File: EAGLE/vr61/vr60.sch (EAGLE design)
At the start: 227 parts, among them IC1 MC74VHC1G50, IC2 REG1117, J3 JTAG, J6 MICROMOD-2222-C

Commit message: pcb tracing done
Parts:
- J3: value JTAG -> (none); device SparkFun-Connectors:CORTEX_JTAG_DEBUG_MINIMUM_PTH -> SparkFun-Connectors:CONN_04
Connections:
- new net A0: J3.3, J6.A0
- new net PWM: J3.2, J6.PWM0
- net !RESET: no longer J3.!RESET
- net GND: now also J3.1; no longer J3.GND
- net SWDCK: no longer J3.SWDCLK
- net SWDIO: no longer J3.SWDIO
- net VCC: now also J3.4; no longer J3.VCC
- net VSUP: now also J6.USB_VIN
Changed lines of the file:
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@@
 <part name="JP1" library="SparkFun-Jumpers" library_urn="urn:adsk.eagle:library:528" deviceset="JUMPER-SMT_2_NC_PASTE" device="_NO-SILK" package3d_urn="urn:adsk.eagle:package:39283/1" value="OPT"/>
 <part name="J1" library="SparkFun-Connectors" library_urn="urn:adsk.eagle:library:513" deviceset="CONN_02" device="" package3d_urn="urn:adsk.eagle:package:38039/1"/>
-<part name="J3" library="SparkFun-Connectors" deviceset="CORTEX_JTAG_DEBUG_MINIMUM" device="_PTH" value="JTAG"/>
 <part name="GND10" library="ts_custom_nick_nacks" deviceset="GND" device=""/>
-<part name="GND11" library="ts_custom_nick_nacks" deviceset="GND" device=""/>
-<part name="U$18" library="ts_custom_nick_nacks" deviceset="3V3" device=""/>
+<part name="J3" library="SparkFun-Connectors" library_urn="urn:adsk.eagle:library:513" deviceset="CONN_04" device="" package3d_urn="urn:adsk.eagle:package:38085/1"/>
+<part name="U$4" library="ts_custom_nick_nacks" deviceset="3V3" device=""/>
+<part name="GND5" library="ts_custom_nick_nacks" deviceset="GND" device=""/>
 </parts>
 <sheets>
@@
 <attribute name="NAME" x="261.62" y="162.052" size="1.778" layer="95" font="vector" rot="R180"/>
 </instance>
-<instance part="J3" gate="G$1" x="241.3" y="50.8" smashed="yes" rot="R180">
-<attribute name="NAME" x="251.46" y="42.926" size="1.778" layer="95" font="vector" rot="R180"/>
-<attribute name="VALUE" x="251.46" y="58.166" size="1.778" layer="96" font="vector" rot="R180"/>
-</instance>
 <instance part="GND10" gate="1" x="248.92" y="162.56" smashed="yes">
 <attribute name="VALUE" x="248.92" y="157.988" size="1.778" layer="96" align="top-center"/>
 </instance>
-<instance part="GND11" gate="1" x="261.62" y="50.8" smashed="yes">
-<attribute name="VALUE" x="261.62" y="46.228" size="1.778" layer="96" align="top-center"/>
-</instance>
-<instance part="U$18" gate="G$1" x="256.54" y="43.18" smashed="yes" rot="R180">
-<attribute name="VALUE" x="256.54" y="38.608" size="1.778" layer="96" rot="R180" align="bottom-center"/>
+<instance part="J3" gate="G$1" x="241.3" y="55.88" smashed="yes">
+<attribute name="VALUE" x="236.22" y="48.514" size="1.778" layer="96" font="vector"/>
+<attribute name="NAME" x="236.22" y="64.008" size="1.778" layer="95" font="vector"/>
+</instance>
+<instance part="U$4" gate="G$1" x="248.92" y="63.5" smashed="yes">
+<attribute name="VALUE" x="248.92" y="68.072" size="1.778" layer="96" align="bottom-center"/>
+</instance>
+<instance part="GND5" gate="1" x="248.92" y="50.8" smashed="yes">
+<attribute name="VALUE" x="248.92" y="46.228" size="1.778" layer="96" align="top-center"/>
 </instance>
 </instances>
@@
 </segment>
 <segment>
-<pinref part="J3" gate="G$1" pin="GND"/>
-<pinref part="GND11" gate="1" pin="GND"/>
-<wire x1="261.62" y1="50.8" x2="261.62" y2="53.34" width="0.1524" layer="91"/>
-<wire x1="261.62" y1="53.34" x2="254" y2="53.34" width="0.1524" layer="91"/>
-</segment>
-<segment>
 <pinref part="J1" gate="G$1" pin="2"/>
 <wire x1="251.46" y1="165.1" x2="248.92" y2="165.1" width="0.1524" layer="91"/>
 <pinref part="GND10" gate="1" pin="GND"/>
 <wire x1="248.92" y1="165.1" x2="248.92" y2="162.56" width="0.1524" layer="91"/>
+</segment>
+<segment>
+<pinref part="J3" gate="G$1" pin="1"/>
+<wire x1="246.38" y1="53.34" x2="248.92" y2="53.34" width="0.1524" layer="91"/>
+<pinref part="GND5" gate="1" pin="GND"/>
+<wire x1="248.92" y1="53.34" x2="248.92" y2="50.8" width="0.1524" layer="91"/>
 </segment>
 </net>
@@
 </segment>
 <segment>
-<pinref part="J3" gate="G$1" pin="VCC"/>
-<wire x1="254" y1="45.72" x2="256.54" y2="45.72" width="0.1524" layer="91"/>
-<wire x1="256.54" y1="45.72" x2="256.54" y2="43.18" width="0.1524" layer="91"/>
-<pinref part="U$18" gate="G$1" pin="VCC"/>
+<pinref part="J3" gate="G$1" pin="4"/>
+<wire x1="246.38" y1="60.96" x2="248.92" y2="60.96" width="0.1524" layer="91"/>
+<pinref part="U$4" gate="G$1" pin="VCC"/>
+<wire x1="248.92" y1="60.96" x2="248.92" y2="63.5" width="0.1524" layer="91"/>
 </segment>
 </net>
@@
 <segment>
 <pinref part="J6" gate="J1" pin="AUD_OUT/CAM_MCLK"/>
-<wire x1="177.8" y1="106.68" x2="160.02" y2="106.68" width="0.1524" layer="91"/>
-<label x="160.02" y="106.68" size="1.778" layer="95" rot="R180" xref="yes"/>
+<wire x1="177.8" y1="106.68" x2="157.48" y2="106.68" width="0.1524" layer="91"/>
+<label x="157.48" y="106.68" size="1.778" layer="95" rot="R180" xref="yes"/>
 </segment>
 </net>
@@
 <segment>
 <pinref part="J6" gate="J1" pin="AUD_LRCLK"/>
-<wire x1="177.8" y1="101.6" x2="160.02" y2="101.6" width="0.1524" layer="91"/>
-<label x="160.02" y="101.6" size="1.778" layer="95" rot="R180" xref="yes"/>
+<wire x1="177.8" y1="101.6" x2="157.48" y2="101.6" width="0.1524" layer="91"/>
+<label x="157.48" y="101.6" size="1.778" layer="95" rot="R180" xref="yes"/>
 </segment>
 </net>
@@
 <segment>
 <pinref part="J6" gate="J1" pin="G3/BUS3"/>
-<wire x1="223.52" y1="86.36" x2="241.3" y2="86.36" width="0.1524" layer="91"/>
-<label x="241.3" y="86.36" size="1.778" layer="95" xref="yes"/>
+<wire x1="223.52" y1="86.36" x2="243.84" y2="86.36" width="0.1524" layer="91"/>
+<label x="243.84" y="86.36" size="1.778" layer="95" xref="yes"/>
 </segment>
 </net>
@@
 <segment>
 <pinref part="J6" gate="J1" pin="G1/BUS1"/>
-<wire x1="223.52" y1="91.44" x2="241.3" y2="91.44" width="0.1524" layer="91"/>
-<label x="241.3" y="91.44" size="1.778" layer="95" xref="yes"/>
+<wire x1="223.52" y1="91.44" x2="243.84" y2="91.44" width="0.1524" layer="91"/>
+<label x="243.84" y="91.44" size="1.778" layer="95" xref="yes"/>
 </segment>
 </net>
@@
 <segment>
 <pinref part="J6" gate="J1" pin="D1/CAM_TRIG"/>
-<wire x1="223.52" y1="116.84" x2="241.3" y2="116.84" width="0.1524" layer="91"/>
-<label x="241.3" y="116.84" size="1.778" layer="95" xref="yes"/>
+<wire x1="223.52" y1="116.84" x2="243.84" y2="116.84" width="0.1524" layer="91"/>
+<label x="243.84" y="116.84" size="1.778" layer="95" xref="yes"/>
 </segment>
 </net>
@@
 <segment>
 <pinref part="J6" gate="J1" pin="I2C_SDA"/>
-<wire x1="177.8" y1="91.44" x2="160.02" y2="91.44" width="0.1524" layer="91"/>
-<label x="160.02" y="91.44" size="1.778" layer="95" rot="R180" xref="yes"/>
+<wire x1="177.8" y1="91.44" x2="157.48" y2="91.44" width="0.1524" layer="91"/>
+<label x="157.48" y="91.44" size="1.778" layer="95" rot="R180" xref="yes"/>
 </segment>
 </net>
@@
 <segment>
 <pinref part="J6" gate="J1" pin="RX1"/>
-<wire x1="223.52" y1="109.22" x2="241.3" y2="109.22" width="0.1524" layer="91"/>
-<label x="241.3" y="109.22" size="1.778" layer="95" xref="yes"/>
+<wire x1="223.52" y1="109.22" x2="243.84" y2="109.22" width="0.1524" layer="91"/>
+<label x="243.84" y="109.22" size="1.778" layer="95" xref="yes"/>
 </segment>
 </net>
@@
 <wire x1="60.96" y1="63.5" x2="60.96" y2="66.04" width="0.1524" layer="91"/>
 </segment>
+<segment>
+<pinref part="J6" gate="J1" pin="USB_VIN"/>
+<wire x1="177.8" y1="142.24" x2="160.02" y2="142.24" width="0.1524" layer="91"/>
+<label x="160.02" y="142.24" size="1.778" layer="95" rot="MR0" xref="yes"/>
+</segment>
 </net>
 <net name="N$67" class="0">
@@
 <segment>
 <pinref part="J6" gate="J1" pin="USB_D-"/>
-<wire x1="177.8" y1="139.7" x2="170.18" y2="139.7" width="0.1524" layer="91"/>
-<label x="170.18" y="139.7" size="1.778" layer="95" rot="R180" xref="yes"/>
+<wire x1="177.8" y1="139.7" x2="167.64" y2="139.7" width="0.1524" layer="91"/>
+<label x="167.64" y="139.7" size="1.778" layer="95" rot="R180" xref="yes"/>
 </segment>
 <segment>
@@
 <segment>
 <pinref part="J6" gate="J1" pin="PWM1"/>
-<wire x1="223.52" y1="121.92" x2="241.3" y2="121.92" width="0.1524" layer="91"/>
-<label x="241.3" y="121.92" size="1.778" layer="95" xref="yes"/>
+<wire x1="223.52" y1="121.92" x2="243.84" y2="121.92" width="0.1524" layer="91"/>
+<label x="243.84" y="121.92" size="1.778" layer="95" xref="yes"/>
 </segment>
 <segment>
@@
 <net name="SWDIO" class="0">
 <segment>
-<label x="220.98" y="48.26" size="1.27" layer="95" rot="R180" xref="yes"/>
-<wire x1="231.14" y1="48.26" x2="220.98" y2="48.26" width="0.1524" layer="91"/>
-<pinref part="J3" gate="G$1" pin="SWDIO"/>
-</segment>
-<segment>
 <pinref part="J6" gate="J1" pin="SWDIO"/>
 <wire x1="177.8" y1="116.84" x2="160.02" y2="116.84" width="0.1524" layer="91"/>
@@
 <net name="SWDCK" class="0">
 <segment>
-<label x="228.6" y="50.8" size="1.27" layer="95" rot="R180" xref="yes"/>
-<wire x1="231.14" y1="50.8" x2="228.6" y2="50.8" width="0.1524" layer="91"/>
-<pinref part="J3" gate="G$1" pin="SWDCLK"/>
-</segment>
-<segment>
 <pinref part="J6" gate="J1" pin="SWDCK"/>
 <wire x1="177.8" y1="114.3" x2="172.72" y2="114.3" width="0.1524" layer="91"/>
@@
 </net>
 <net name="!RESET" class="0">
-<segment>
-<wire x1="231.14" y1="45.72" x2="228.6" y2="45.72" width="0.1524" layer="91"/>
-<label x="228.6" y="45.72" size="1.27" layer="95" rot="R180" xref="yes"/>
-<pinref part="J3" gate="G$1" pin="!RESET"/>
-</segment>
 <segment>
 <pinref part="J6" gate="J1" pin="!RESET!"/>
@@
 </segment>
 </net>
+<net name="PWM" class="0">
+<segment>
+<pinref part="J6" gate="J1" pin="PWM0"/>
+<wire x1="223.52" y1="124.46" x2="251.46" y2="124.46" width="0.1524" layer="91"/>
+<label x="251.46" y="124.46" size="1.778" layer="95" xref="yes"/>
+</segment>
+<segment>
+<pinref part="J3" gate="G$1" pin="2"/>
+<wire x1="246.38" y1="55.88" x2="248.92" y2="55.88" width="0.1524" layer="91"/>
+<label x="248.92" y="55.88" size="1.778" layer="95" xref="yes"/>
+</segment>
+</net>
+<net name="A0" class="0">
+<segment>
+<pinref part="J6" gate="J1" pin="A0"/>
+<wire x1="223.52" y1="129.54" x2="243.84" y2="129.54" width="0.1524" layer="91"/>
+<label x="243.84" y="129.54" size="1.778" layer="95" xref="yes"/>
+</segment>
+<segment>
+<pinref part="J3" gate="G$1" pin="3"/>
+<wire x1="246.38" y1="58.42" x2="259.08" y2="58.42" width="0.1524" layer="91"/>
+<label x="259.08" y="58.42" size="1.778" layer="95" xref="yes"/>
+</segment>
+</net>

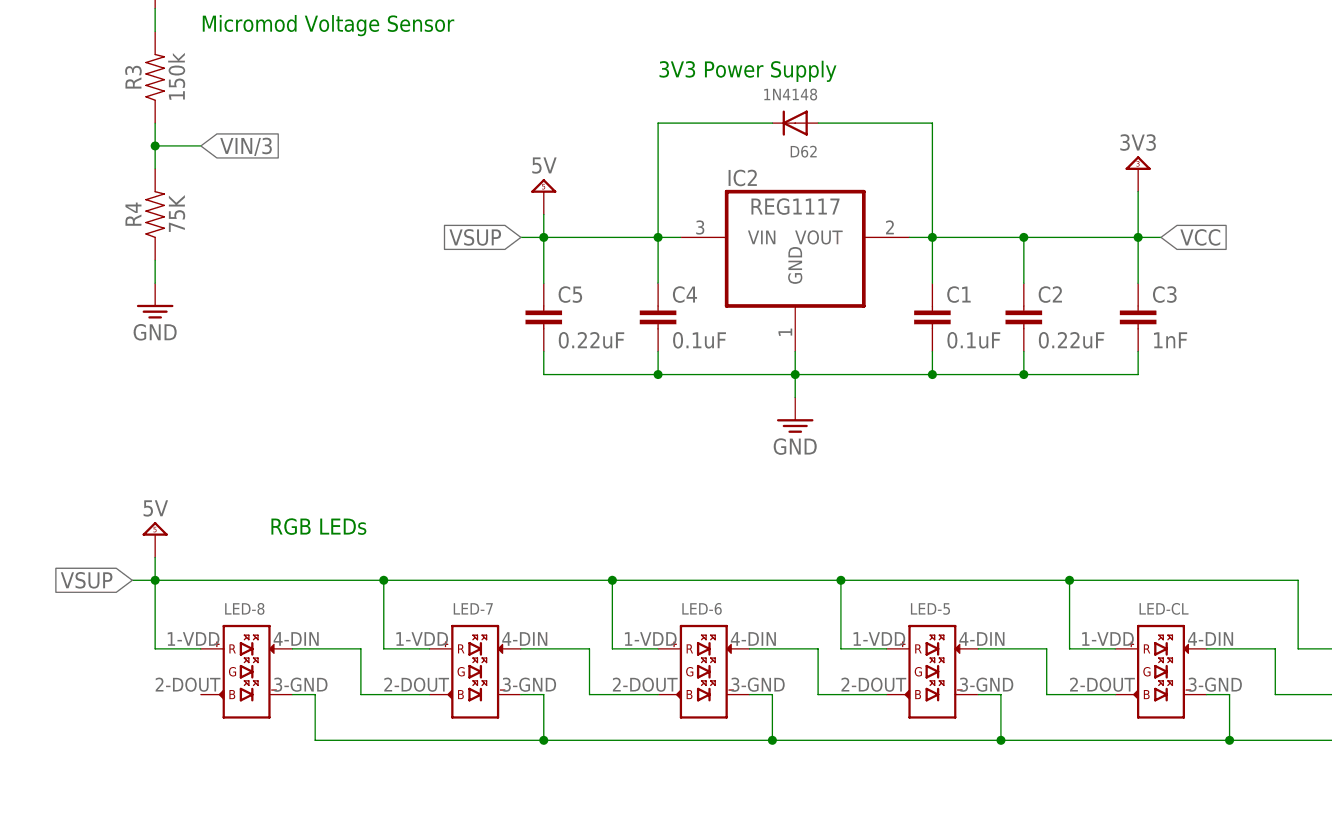
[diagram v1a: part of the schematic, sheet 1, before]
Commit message: added heat sink on 1117
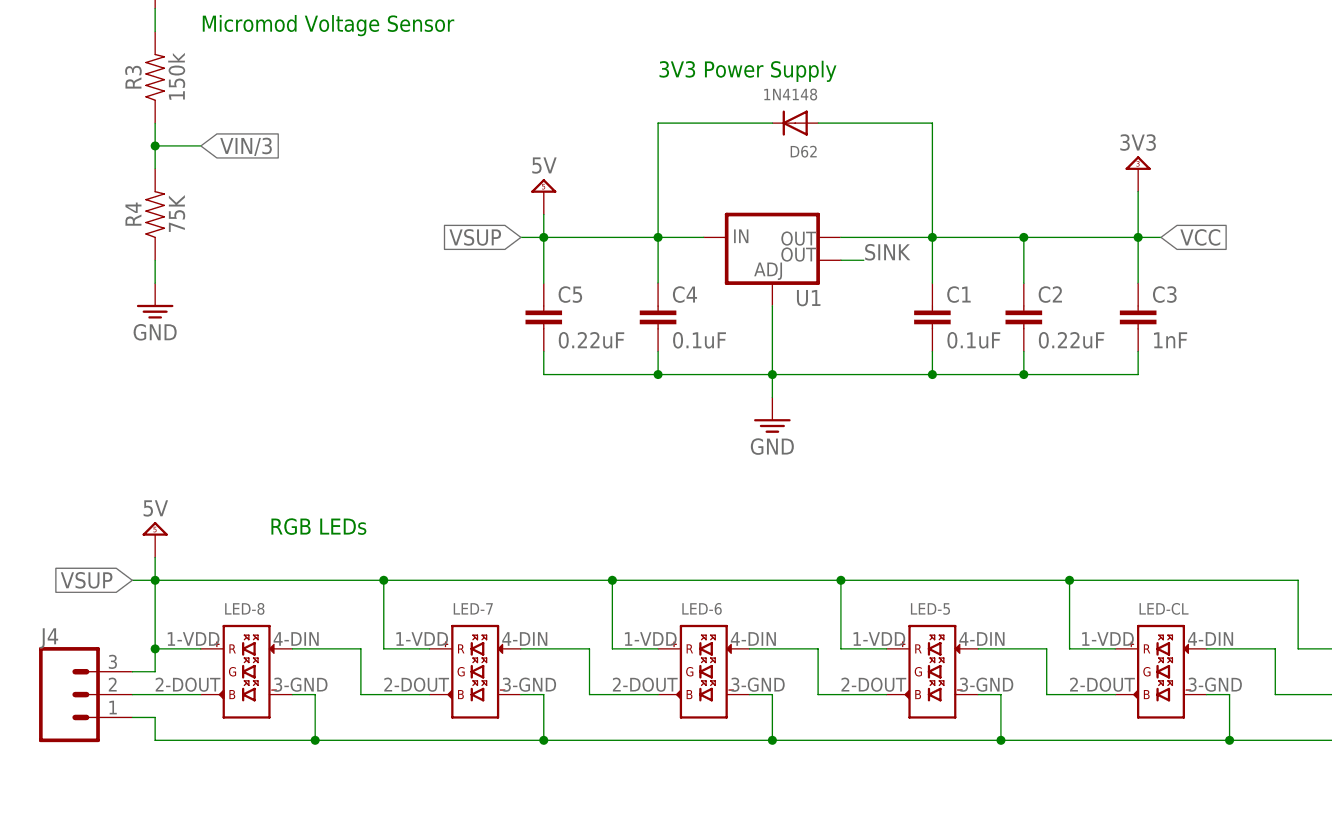
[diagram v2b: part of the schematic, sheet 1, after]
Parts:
- removed IC2: REG1117, burr-brown:REG1117
- added J4: (no value), SparkFun-Connectors:CONN_03
- added U1: (no value), SparkFun-IC-Power:V_REG_LM1117SOT223
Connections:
- new net N$72: J4.2, LED-8.2_DOUT
- new net SINK: U1.OUT@1
- net GND: now also J4.1, U1.ADJ; no longer IC2.GND
- net VCC: now also U1.OUT; no longer IC2.VOUT
- net VSUP: now also J4.3, U1.IN; no longer IC2.VIN
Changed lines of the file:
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@@
 <part name="U$11" library="ts_custom_nick_nacks" deviceset="5V" device=""/>
 <part name="GND4" library="ts_custom_nick_nacks" deviceset="GND" device=""/>
-<part name="IC2" library="burr-brown" library_urn="urn:adsk.eagle:library:111" deviceset="REG1117" device="" package3d_urn="urn:adsk.eagle:package:4940/1"/>
 <part name="U$16" library="ts_custom_nick_nacks" deviceset="3V3" device=""/>
 <part name="C1" library="SparkFun-Capacitors" library_urn="urn:adsk.eagle:library:510" deviceset="0.1UF" device="-0603-25V-5%" package3d_urn="urn:adsk.eagle:package:37414/1" value="0.1uF"/>
@@
 <part name="U$4" library="ts_custom_nick_nacks" deviceset="3V3" device=""/>
 <part name="GND5" library="ts_custom_nick_nacks" deviceset="GND" device=""/>
+<part name="J4" library="SparkFun-Connectors" library_urn="urn:adsk.eagle:library:513" deviceset="CONN_03" device="" package3d_urn="urn:adsk.eagle:package:38063/1"/>
+<part name="U1" library="SparkFun-IC-Power" library_urn="urn:adsk.eagle:library:526" deviceset="V_REG_LM1117" device="SOT223" package3d_urn="urn:adsk.eagle:package:39069/1"/>
 </parts>
 <sheets>
@@
 <attribute name="VALUE" x="40.64" y="117.348" size="1.778" layer="96" align="top-center"/>
 </instance>
-<instance part="IC2" gate="G$1" x="88.9" y="63.5" smashed="yes">
-<attribute name="NAME" x="81.28" y="69.215" size="1.778" layer="95" ratio="10"/>
-<attribute name="VALUE" x="83.82" y="66.04" size="1.778" layer="96" ratio="10"/>
-</instance>
 <instance part="U$16" gate="G$1" x="127" y="68.58" smashed="yes">
 <attribute name="VALUE" x="127" y="73.152" size="1.778" layer="96" align="bottom-center"/>
@@
 <attribute name="VALUE" x="75.184" y="51.181" size="1.778" layer="96" font="vector"/>
 </instance>
-<instance part="GND6" gate="1" x="88.9" y="45.72" smashed="yes">
-<attribute name="VALUE" x="88.9" y="41.148" size="1.778" layer="96" align="top-center"/>
+<instance part="GND6" gate="1" x="86.36" y="45.72" smashed="yes">
+<attribute name="VALUE" x="86.36" y="41.148" size="1.778" layer="96" align="top-center"/>
 </instance>
 <instance part="S1" gate="G$1" x="157.48" y="162.56" smashed="yes">
@@
 <instance part="GND5" gate="1" x="248.92" y="50.8" smashed="yes">
 <attribute name="VALUE" x="248.92" y="46.228" size="1.778" layer="96" align="top-center"/>
+</instance>
+<instance part="J4" gate="J$1" x="7.62" y="12.7" smashed="yes">
+<attribute name="VALUE" x="5.08" y="5.334" size="1.778" layer="96" font="vector"/>
+<attribute name="NAME" x="5.08" y="18.288" size="1.778" layer="95" font="vector"/>
+</instance>
+<instance part="U1" gate="G$1" x="86.36" y="63.5" smashed="yes">
+<attribute name="NAME" x="88.9" y="55.88" size="1.778" layer="95" font="vector"/>
+<attribute name="VALUE" x="88.9" y="53.34" size="1.778" layer="96" font="vector"/>
 </instance>
 </instances>
@@
 <pinref part="C4" gate="G$1" pin="2"/>
 <wire x1="73.66" y1="50.8" x2="73.66" y2="48.26" width="0.1524" layer="91"/>
-<wire x1="73.66" y1="48.26" x2="88.9" y2="48.26" width="0.1524" layer="91"/>
+<wire x1="73.66" y1="48.26" x2="86.36" y2="48.26" width="0.1524" layer="91"/>
 <pinref part="C1" gate="G$1" pin="2"/>
-<wire x1="88.9" y1="48.26" x2="104.14" y2="48.26" width="0.1524" layer="91"/>
+<wire x1="86.36" y1="48.26" x2="104.14" y2="48.26" width="0.1524" layer="91"/>
 <wire x1="104.14" y1="48.26" x2="104.14" y2="50.8" width="0.1524" layer="91"/>
-<pinref part="IC2" gate="G$1" pin="GND"/>
-<wire x1="88.9" y1="50.8" x2="88.9" y2="48.26" width="0.1524" layer="91"/>
-<junction x="88.9" y="48.26"/>
+<junction x="86.36" y="48.26"/>
 <pinref part="GND6" gate="1" pin="GND"/>
-<wire x1="88.9" y1="48.26" x2="88.9" y2="45.72" width="0.1524" layer="91"/>
+<wire x1="86.36" y1="48.26" x2="86.36" y2="45.72" width="0.1524" layer="91"/>
 <pinref part="C5" gate="G$1" pin="2"/>
 <wire x1="60.96" y1="50.8" x2="60.96" y2="48.26" width="0.1524" layer="91"/>
@@
 <wire x1="114.3" y1="48.26" x2="114.3" y2="50.8" width="0.1524" layer="91"/>
 <junction x="114.3" y="48.26"/>
+<pinref part="U1" gate="G$1" pin="ADJ"/>
+<wire x1="86.36" y1="55.88" x2="86.36" y2="48.26" width="0.1524" layer="91"/>
 </segment>
 <segment>
@@
 <wire x1="167.64" y1="12.7" x2="167.64" y2="10.16" width="0.1524" layer="91"/>
 <junction x="167.64" y="10.16"/>
+<pinref part="J4" gate="J$1" pin="1"/>
+<wire x1="15.24" y1="10.16" x2="17.78" y2="10.16" width="0.1524" layer="91"/>
+<wire x1="17.78" y1="10.16" x2="17.78" y2="7.62" width="0.1524" layer="91"/>
+<wire x1="17.78" y1="7.62" x2="35.56" y2="7.62" width="0.1524" layer="91"/>
+<junction x="35.56" y="7.62"/>
 </segment>
 <segment>
@@
 </segment>
 <segment>
-<pinref part="IC2" gate="G$1" pin="VOUT"/>
-<wire x1="101.6" y1="63.5" x2="104.14" y2="63.5" width="0.1524" layer="91"/>
 <pinref part="C1" gate="G$1" pin="1"/>
 <wire x1="104.14" y1="63.5" x2="104.14" y2="58.42" width="0.1524" layer="91"/>
@@
 <pinref part="D62" gate="G$1" pin="A"/>
 <wire x1="104.14" y1="76.2" x2="91.44" y2="76.2" width="0.1524" layer="91"/>
+<pinref part="U1" gate="G$1" pin="OUT"/>
+<wire x1="93.98" y1="63.5" x2="104.14" y2="63.5" width="0.1524" layer="91"/>
 </segment>
 <segment>
@@
 <pinref part="IC1" gate="G$1" pin="5_VCC"/>
 <wire x1="144.78" y1="17.78" x2="149.86" y2="17.78" width="0.1524" layer="91"/>
+<pinref part="J4" gate="J$1" pin="3"/>
+<wire x1="15.24" y1="15.24" x2="17.78" y2="15.24" width="0.1524" layer="91"/>
+<wire x1="17.78" y1="15.24" x2="17.78" y2="17.78" width="0.1524" layer="91"/>
+<junction x="17.78" y="17.78"/>
 </segment>
 <segment>
@@
 </segment>
 <segment>
-<pinref part="IC2" gate="G$1" pin="VIN"/>
-<wire x1="76.2" y1="63.5" x2="73.66" y2="63.5" width="0.1524" layer="91"/>
 <wire x1="73.66" y1="63.5" x2="60.96" y2="63.5" width="0.1524" layer="91"/>
 <junction x="73.66" y="63.5"/>
@@
 <pinref part="U$9" gate="G$1" pin="VCC"/>
 <wire x1="60.96" y1="63.5" x2="60.96" y2="66.04" width="0.1524" layer="91"/>
+<pinref part="U1" gate="G$1" pin="IN"/>
+<wire x1="78.74" y1="63.5" x2="73.66" y2="63.5" width="0.1524" layer="91"/>
 </segment>
 <segment>
@@
 </segment>
 </net>
+<net name="N$72" class="0">
+<segment>
+<pinref part="LED-8" gate="G$1" pin="2_DOUT"/>
+<pinref part="J4" gate="J$1" pin="2"/>
+<wire x1="22.86" y1="12.7" x2="15.24" y2="12.7" width="0.1524" layer="91"/>
+</segment>
+</net>
+<net name="SINK" class="0">
+<segment>
+<pinref part="U1" gate="G$1" pin="OUT@1"/>
+<wire x1="93.98" y1="60.96" x2="96.52" y2="60.96" width="0.1524" layer="91"/>
+<label x="96.52" y="60.96" size="1.778" layer="95"/>
+</segment>
+</net>
